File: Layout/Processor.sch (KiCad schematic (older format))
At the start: 5 parts

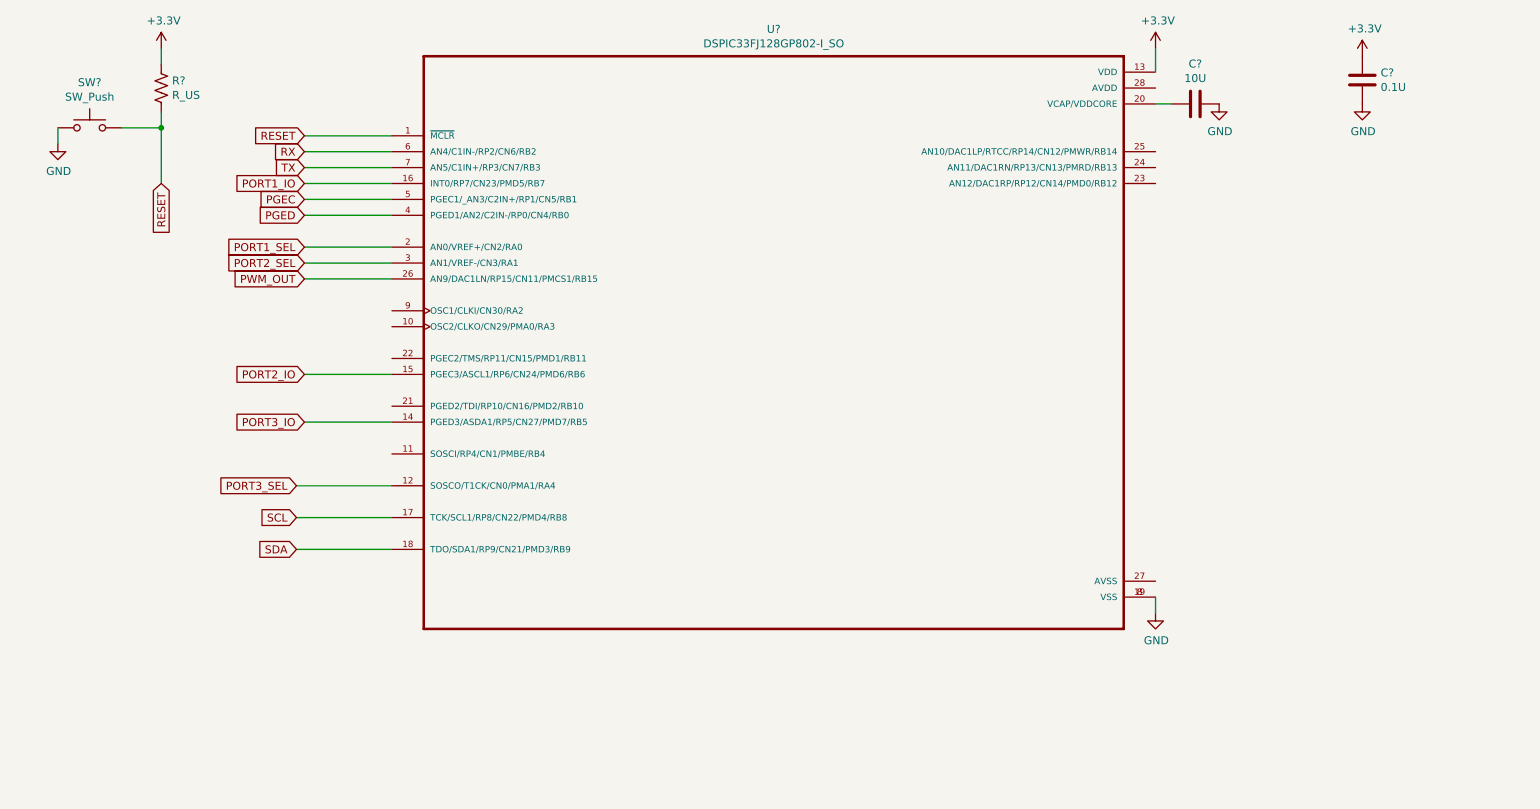
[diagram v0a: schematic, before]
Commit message: Add more sheets. Add LEDs
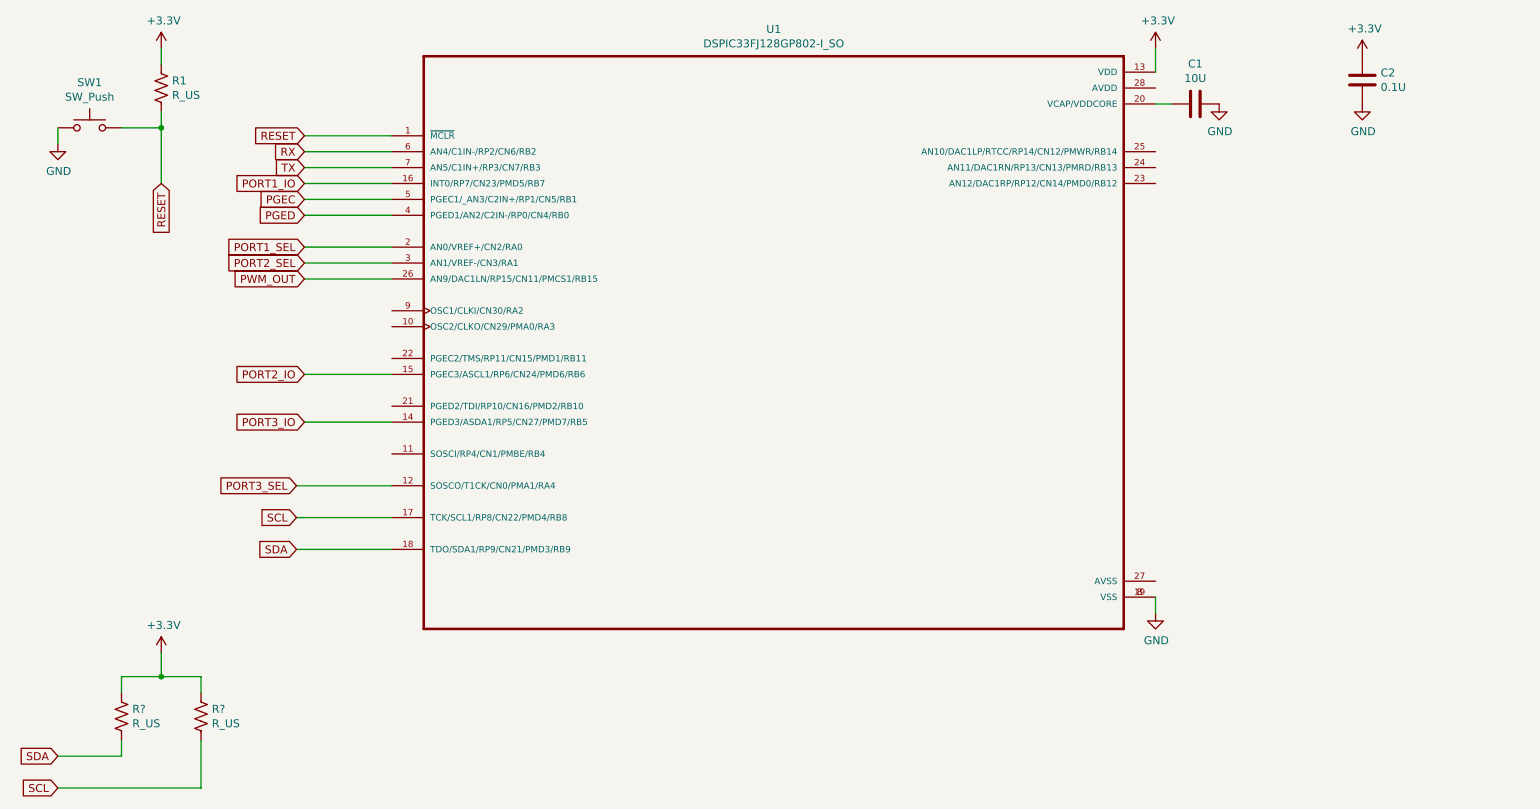
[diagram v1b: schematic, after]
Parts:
- added R? (x2): R_US, symbol Device:R_US
- gave numbers to parts that had none: 5
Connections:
- net +3V3: now also R?.1, R?.1
- net SCL: now also R?.2
- net SDA: now also R?.2
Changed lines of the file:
@@
 $Descr A4 11693 8268
 encoding utf-8
-Sheet 2 4
+Sheet 2 7
 Title ""
 Date ""
@@
 $EndDescr
 $Comp
-L Switch:SW_Push SW?
+L Switch:SW_Push SW1
 U 1 1 5F35733D
 P 1500 1650
-F 0 "SW?" H 1500 1935 50  0000 C CNN
+F 0 "SW1" H 1500 1935 50  0000 C CNN
 F 1 "SW_Push" H 1500 1844 50  0000 C CNN
 F 2 "" H 1500 1850 50  0001 C CNN
@@
 $EndComp
 $Comp
-L Device:R_US R?
+L Device:R_US R1
 U 1 1 5F357DB5
 P 1950 1400
-F 0 "R?" H 2018 1446 50  0000 L CNN
+F 0 "R1" H 2018 1446 50  0000 L CNN
 F 1 "R_US" H 2018 1355 50  0000 L CNN
 F 2 "" V 1990 1390 50  0001 C CNN
@@
 Connection ~ 1950 1650
 $Comp
-L power:GND #PWR?
+L power:GND #PWR0101
 U 1 1 5F358880
 P 1300 1750
-F 0 "#PWR?" H 1300 1500 50  0001 C CNN
+F 0 "#PWR0101" H 1300 1500 50  0001 C CNN
 F 1 "GND" H 1305 1577 50  0000 C CNN
 F 2 "" H 1300 1750 50  0001 C CNN
@@
 	1300 1750 1300 1650
 $Comp
-L power:+3.3V #PWR?
+L power:+3.3V #PWR0102
 U 1 1 5F358F61
 P 1950 1150
-F 0 "#PWR?" H 1950 1000 50  0001 C CNN
+F 0 "#PWR0102" H 1950 1000 50  0001 C CNN
 F 1 "+3.3V" H 1965 1323 50  0000 C CNN
 F 2 "" H 1950 1150 50  0001 C CNN
@@
 RESET
 $Comp
-L DSPIC33FJ128GP802-I_SO:DSPIC33FJ128GP802-I_SO U?
+L DSPIC33FJ128GP802-I_SO:DSPIC33FJ128GP802-I_SO U1
 U 1 1 5F360275
 P 5800 3000
-F 0 "U?" H 5800 4970 50  0000 C CNN
+F 0 "U1" H 5800 4970 50  0000 C CNN
 F 1 "DSPIC33FJ128GP802-I_SO" H 5800 4879 50  0000 C CNN
 F 2 "SOIC127P1030X265-28N" H 5800 3000 50  0001 L BNN
@@
 RESET
 $Comp
-L Device:C C?
+L Device:C C1
 U 1 1 5F36AEA4
 P 8450 1500
-F 0 "C?" V 8198 1500 50  0000 C CNN
+F 0 "C1" V 8198 1500 50  0000 C CNN
 F 1 "10U" V 8289 1500 50  0000 C CNN
 F 2 "" H 8488 1350 50  0001 C CNN
@@
 	8200 1500 8300 1500
 $Comp
-L power:+3.3V #PWR?
+L power:+3.3V #PWR0103
 U 1 1 5F36B77A
 P 8200 1150
-F 0 "#PWR?" H 8200 1000 50  0001 C CNN
+F 0 "#PWR0103" H 8200 1000 50  0001 C CNN
 F 1 "+3.3V" H 8215 1323 50  0000 C CNN
 F 2 "" H 8200 1150 50  0001 C CNN
@@
 	8200 1150 8200 1300
 $Comp
-L power:GND #PWR?
+L power:GND #PWR0104
 U 1 1 5F36C154
 P 8600 1500
-F 0 "#PWR?" H 8600 1250 50  0001 C CNN
+F 0 "#PWR0104" H 8600 1250 50  0001 C CNN
 F 1 "GND" H 8605 1327 50  0000 C CNN
 F 2 "" H 8600 1500 50  0001 C CNN
@@
 $EndComp
 $Comp
-L power:GND #PWR?
+L power:GND #PWR0105
 U 1 1 5F36C44E
 P 8200 4700
-F 0 "#PWR?" H 8200 4450 50  0001 C CNN
+F 0 "#PWR0105" H 8200 4450 50  0001 C CNN
 F 1 "GND" H 8205 4527 50  0000 C CNN
 F 2 "" H 8200 4700 50  0001 C CNN
@@
 PORT3_SEL
 $Comp
-L Device:C C?
+L Device:C C2
 U 1 1 5F36FE4F
 P 9500 1350
-F 0 "C?" H 9615 1396 50  0000 L CNN
+F 0 "C2" H 9615 1396 50  0000 L CNN
 F 1 "0.1U" H 9615 1305 50  0000 L CNN
 F 2 "" H 9538 1200 50  0001 C CNN
@@
 $EndComp
 $Comp
-L power:+3.3V #PWR?
+L power:+3.3V #PWR0106
 U 1 1 5F370E83
 P 9500 1200
-F 0 "#PWR?" H 9500 1050 50  0001 C CNN
+F 0 "#PWR0106" H 9500 1050 50  0001 C CNN
 F 1 "+3.3V" H 9515 1373 50  0000 C CNN
 F 2 "" H 9500 1200 50  0001 C CNN
@@
 $EndComp
 $Comp
-L power:GND #PWR?
+L power:GND #PWR0107
 U 1 1 5F3712C2
 P 9500 1500
-F 0 "#PWR?" H 9500 1250 50  0001 C CNN
+F 0 "#PWR0107" H 9500 1250 50  0001 C CNN
 F 1 "GND" H 9505 1327 50  0000 C CNN
 F 2 "" H 9500 1500 50  0001 C CNN
@@
 	1    0    0    -1
 $EndComp
+$Comp
+L Device:R_US R?
+U 1 1 5F39076D
+P 1700 5350
+F 0 "R?" H 1768 5396 50  0000 L CNN
+F 1 "R_US" H 1768 5305 50  0000 L CNN
+F 2 "" V 1740 5340 50  0001 C CNN
+F 3 "~" H 1700 5350 50  0001 C CNN
+	1    1700 5350
+	1    0    0    -1
+$EndComp
+$Comp
+L Device:R_US R?
+U 1 1 5F3923D8
+P 2200 5350
+F 0 "R?" H 2268 5396 50  0000 L CNN
+F 1 "R_US" H 2268 5305 50  0000 L CNN
+F 2 "" V 2240 5340 50  0001 C CNN
+F 3 "~" H 2200 5350 50  0001 C CNN
+	1    2200 5350
+	1    0    0    -1
+$EndComp
+Wire Wire Line
+	1700 5200 1700 5100
+Wire Wire Line
+	1700 5100 1950 5100
+Wire Wire Line
+	2200 5100 2200 5200
+Text GLabel 1300 5600 0    50   Input ~ 0
+SDA
+Text GLabel 1300 5800 0    50   Input ~ 0
+SCL
+Wire Wire Line
+	1300 5600 1700 5600
+Wire Wire Line
+	1700 5600 1700 5500
+Wire Wire Line
+	1300 5800 2200 5800
+Wire Wire Line
+	2200 5800 2200 5500
+$Comp
+L power:+3.3V #PWR?
+U 1 1 5F3937F3
+P 1950 4950
+F 0 "#PWR?" H 1950 4800 50  0001 C CNN
+F 1 "+3.3V" H 1965 5123 50  0000 C CNN
+F 2 "" H 1950 4950 50  0001 C CNN
+F 3 "" H 1950 4950 50  0001 C CNN
+	1    1950 4950
+	1    0    0    -1
+$EndComp
+Wire Wire Line
+	1950 4950 1950 5100
+Connection ~ 1950 5100
+Wire Wire Line
+	1950 5100 2200 5100
 $EndSCHEMATC

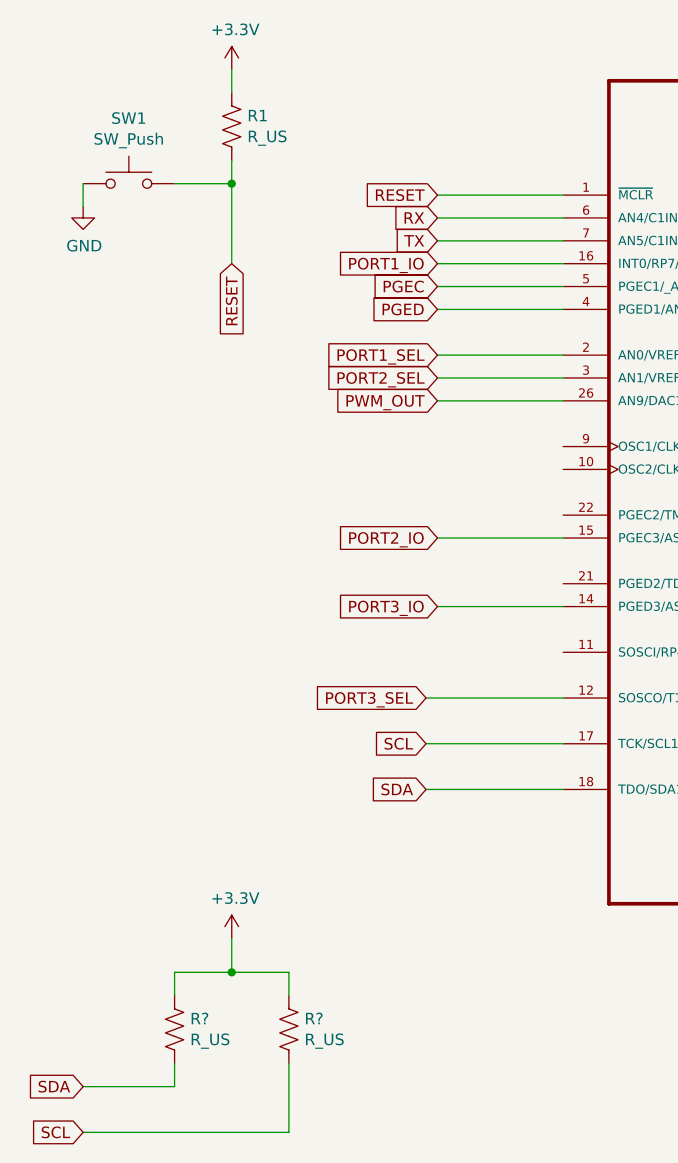
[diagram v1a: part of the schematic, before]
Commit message: Add voltage regulators
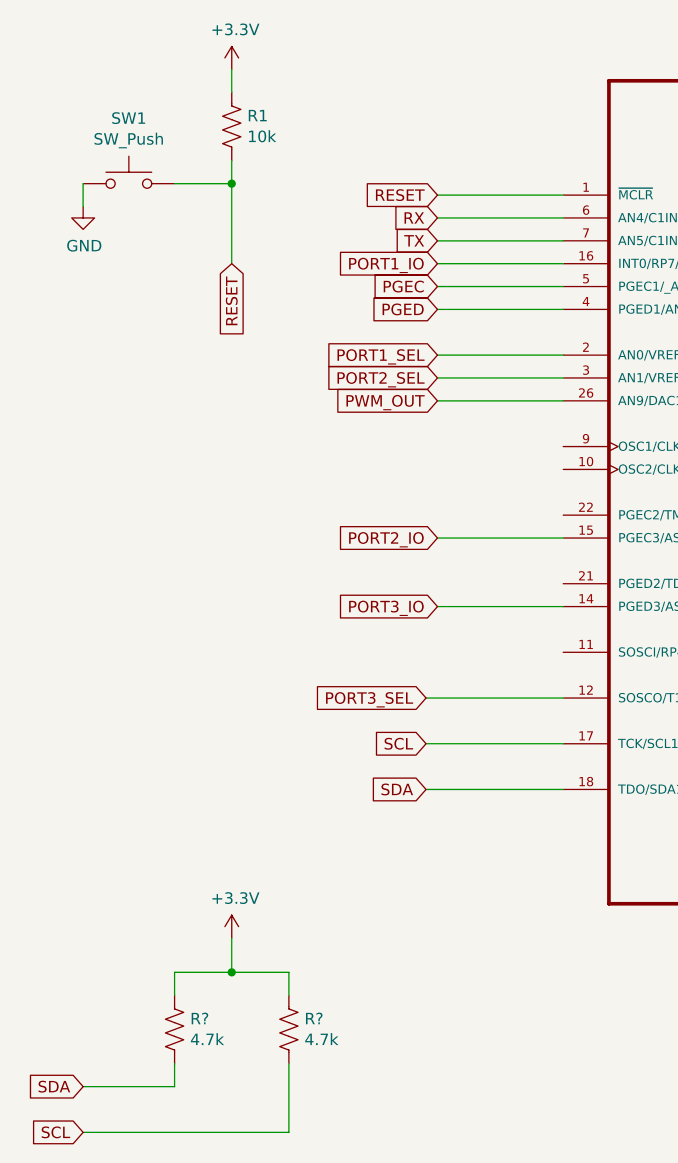
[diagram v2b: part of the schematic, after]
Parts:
- R1: value R_US -> 10k
- R? (x2): value R_US -> 4.7k
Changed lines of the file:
@@
 P 1950 1400
 F 0 "R1" H 2018 1446 50  0000 L CNN
-F 1 "R_US" H 2018 1355 50  0000 L CNN
+F 1 "10k" H 2018 1355 50  0000 L CNN
 F 2 "" V 1990 1390 50  0001 C CNN
 F 3 "~" H 1950 1400 50  0001 C CNN
@@
 P 1700 5350
 F 0 "R?" H 1768 5396 50  0000 L CNN
-F 1 "R_US" H 1768 5305 50  0000 L CNN
+F 1 "4.7k" H 1768 5305 50  0000 L CNN
 F 2 "" V 1740 5340 50  0001 C CNN
 F 3 "~" H 1700 5350 50  0001 C CNN
@@
 P 2200 5350
 F 0 "R?" H 2268 5396 50  0000 L CNN
-F 1 "R_US" H 2268 5305 50  0000 L CNN
+F 1 "4.7k" H 2268 5305 50  0000 L CNN
 F 2 "" V 2240 5340 50  0001 C CNN
 F 3 "~" H 2200 5350 50  0001 C CNN

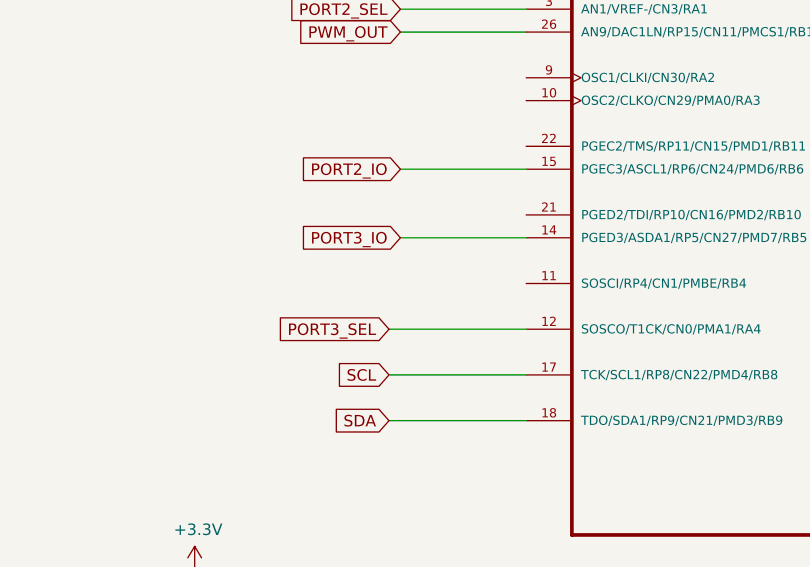
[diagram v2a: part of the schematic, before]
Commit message: Add memory
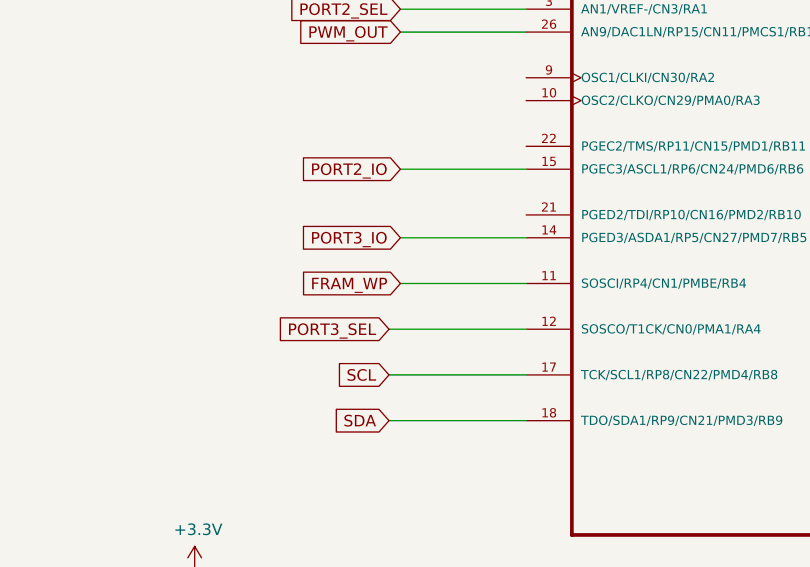
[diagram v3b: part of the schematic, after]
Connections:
- net FRAM_WP: now reaches U1.11 (SOSCI/RP4/CN1/PMBE/RB4)
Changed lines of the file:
@@
 Wire Wire Line
 	1950 5100 2200 5100
+Text GLabel 2850 3700 0    50   Input ~ 0
+FRAM_WP
+Wire Wire Line
+	2850 3700 3400 3700
 $EndSCHEMATC

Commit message: Add footprints
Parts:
- C1, C2: footprint (none) -> Capacitor_SMD:C_0603_1608Metric_Pad1.05x0.95mm_HandSolder
- R1, R? (x2): footprint (none) -> Resistor_SMD:R_0603_1608Metric_Pad1.05x0.95mm_HandSolder
- SW1: footprint (none) -> Button_Switch_SMD:SW_SPST_TL3342
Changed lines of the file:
@@
 F 0 "SW1" H 1500 1935 50  0000 C CNN
 F 1 "SW_Push" H 1500 1844 50  0000 C CNN
-F 2 "" H 1500 1850 50  0001 C CNN
+F 2 "Button_Switch_SMD:SW_SPST_TL3342" H 1500 1850 50  0001 C CNN
 F 3 "~" H 1500 1850 50  0001 C CNN
 	1    1500 1650
@@
 F 0 "R1" H 2018 1446 50  0000 L CNN
 F 1 "10k" H 2018 1355 50  0000 L CNN
-F 2 "" V 1990 1390 50  0001 C CNN
+F 2 "Resistor_SMD:R_0603_1608Metric_Pad1.05x0.95mm_HandSolder" V 1990 1390 50  0001 C CNN
 F 3 "~" H 1950 1400 50  0001 C CNN
 	1    1950 1400
@@
 F 0 "C1" V 8198 1500 50  0000 C CNN
 F 1 "10U" V 8289 1500 50  0000 C CNN
-F 2 "" H 8488 1350 50  0001 C CNN
+F 2 "Capacitor_SMD:C_0603_1608Metric_Pad1.05x0.95mm_HandSolder" H 8488 1350 50  0001 C CNN
 F 3 "~" H 8450 1500 50  0001 C CNN
 	1    8450 1500
@@
 F 0 "C2" H 9615 1396 50  0000 L CNN
 F 1 "0.1U" H 9615 1305 50  0000 L CNN
-F 2 "" H 9538 1200 50  0001 C CNN
+F 2 "Capacitor_SMD:C_0603_1608Metric_Pad1.05x0.95mm_HandSolder" H 9538 1200 50  0001 C CNN
 F 3 "~" H 9500 1350 50  0001 C CNN
 	1    9500 1350
@@
 F 0 "R?" H 1768 5396 50  0000 L CNN
 F 1 "4.7k" H 1768 5305 50  0000 L CNN
-F 2 "" V 1740 5340 50  0001 C CNN
+F 2 "Resistor_SMD:R_0603_1608Metric_Pad1.05x0.95mm_HandSolder" V 1740 5340 50  0001 C CNN
 F 3 "~" H 1700 5350 50  0001 C CNN
 	1    1700 5350
@@
 F 0 "R?" H 2268 5396 50  0000 L CNN
 F 1 "4.7k" H 2268 5305 50  0000 L CNN
-F 2 "" V 2240 5340 50  0001 C CNN
+F 2 "Resistor_SMD:R_0603_1608Metric_Pad1.05x0.95mm_HandSolder" V 2240 5340 50  0001 C CNN
 F 3 "~" H 2200 5350 50  0001 C CNN
 	1    2200 5350

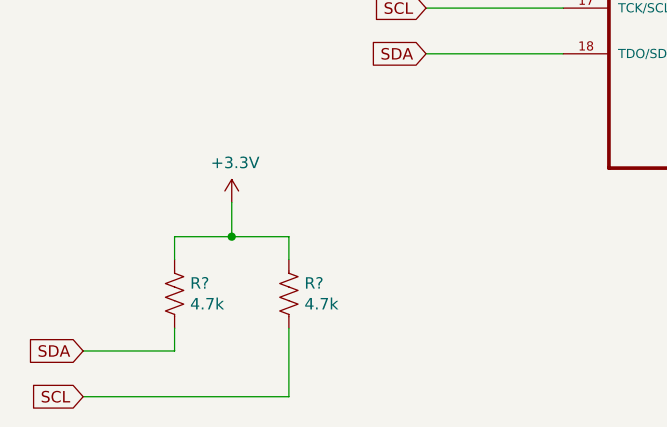
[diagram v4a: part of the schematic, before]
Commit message: Update footprints and references
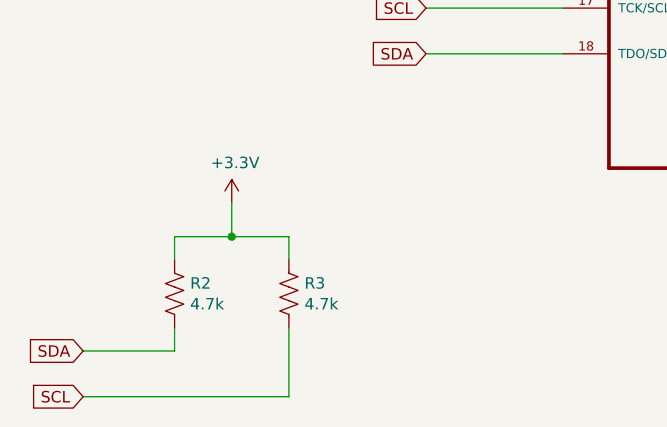
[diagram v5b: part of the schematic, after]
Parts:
- gave numbers to parts that had none: 2
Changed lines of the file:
@@
 $EndComp
 $Comp
-L Device:R_US R?
+L Device:R_US R2
 U 1 1 5F39076D
 P 1700 5350
-F 0 "R?" H 1768 5396 50  0000 L CNN
+F 0 "R2" H 1768 5396 50  0000 L CNN
 F 1 "4.7k" H 1768 5305 50  0000 L CNN
 F 2 "Resistor_SMD:R_0603_1608Metric_Pad1.05x0.95mm_HandSolder" V 1740 5340 50  0001 C CNN
@@
 $EndComp
 $Comp
-L Device:R_US R?
+L Device:R_US R3
 U 1 1 5F3923D8
 P 2200 5350
-F 0 "R?" H 2268 5396 50  0000 L CNN
+F 0 "R3" H 2268 5396 50  0000 L CNN
 F 1 "4.7k" H 2268 5305 50  0000 L CNN
 F 2 "Resistor_SMD:R_0603_1608Metric_Pad1.05x0.95mm_HandSolder" V 2240 5340 50  0001 C CNN
@@
 	2200 5800 2200 5500
 $Comp
-L power:+3.3V #PWR?
+L power:+3.3V #PWR0116
 U 1 1 5F3937F3
 P 1950 4950
-F 0 "#PWR?" H 1950 4800 50  0001 C CNN
+F 0 "#PWR0116" H 1950 4800 50  0001 C CNN
 F 1 "+3.3V" H 1965 5123 50  0000 C CNN
 F 2 "" H 1950 4950 50  0001 C CNN
